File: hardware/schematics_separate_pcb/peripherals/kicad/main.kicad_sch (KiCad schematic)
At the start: 41 parts, among them IC110 74245N, IC113 7404N, IC116 74138N, IC122 7420N, IC162 7430N, IC165 7427N, IC172 74244N, IC173 74244N, IC174 74244N, IC176 74138N, IC188 7432N, IC197 74244N, IC199 74138N, IC35 7408N, IC43 7404N, IC86 74138N, J1 Conn_02x17_Odd_Even, J2 DIN41612_03x32_C_Split, J3 Conn_02x25_Odd_Even_MountingP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, U1 AS6C4008-55PCN, U10 8253, U12 74LS377, U13 16550, U14 16550, U15 AS6C4008-55PCN, U16 27C512, U17 M48Tx2, U2 AS6C4008-55PCN, U20 74LS244, U22 74HCT244, U3 AS6C4008-55PCN, U4 AS6C4008-55PCN, U5 AS6C4008-55PCN, U6 AS6C4008-55PCN, U7 AS6C4008-55PCN, U8 CY62256-70PC, X2 8mhz_osc

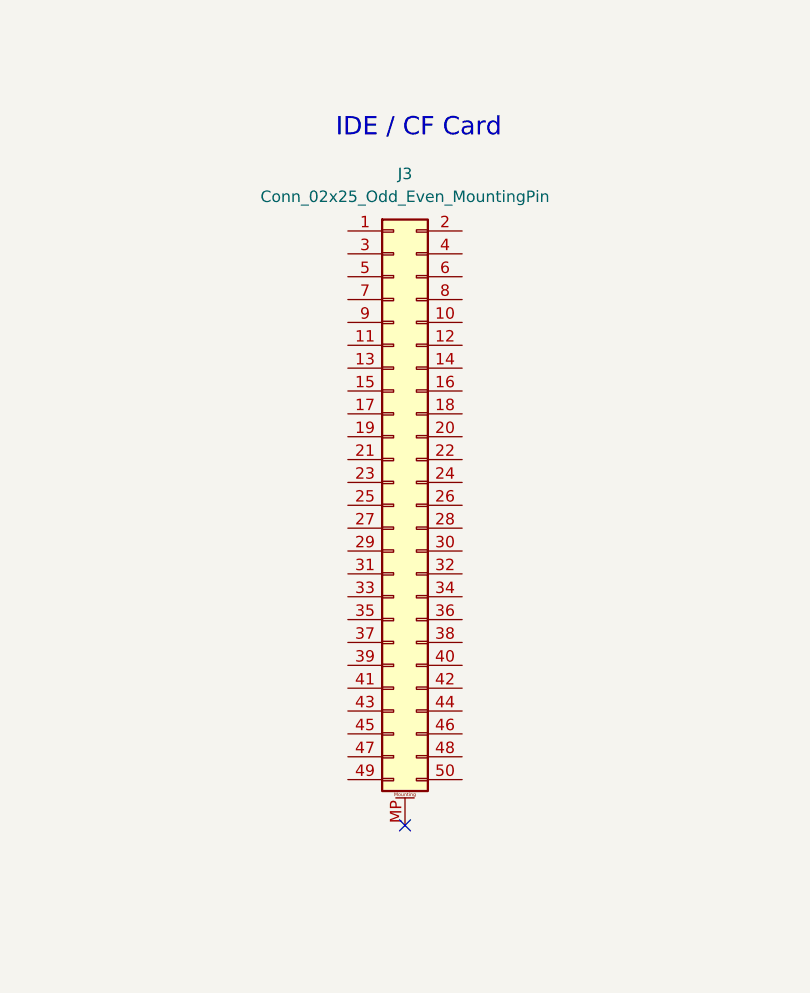
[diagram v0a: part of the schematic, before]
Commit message: improve emulator with -O3 flag
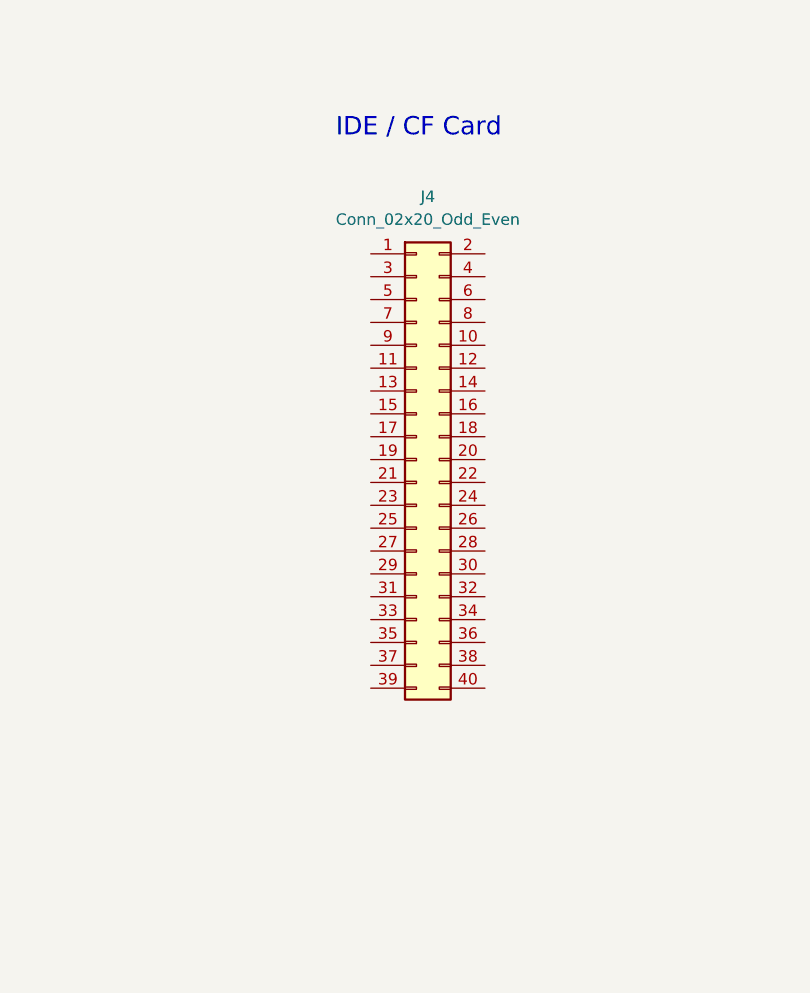
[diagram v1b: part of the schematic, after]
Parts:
- removed J3: Conn_02x25_Odd_Even_MountingPin, symbol Connector_Generic_MountingPin:Conn_02x25_Odd_Even_MountingPin
- added unit 2 of IC110
- added unit 3 of IC113
- added unit 2 of IC113
- added unit 5 of IC113
- added unit 6 of IC113
- added unit 7 of IC113
- added unit 2 of IC116
- added unit 2 of IC122
- added unit 3 of IC122
- added unit 2 of IC162
- added unit 4 of IC165
- added unit 3 of IC165
- added unit 3 of IC172
- added unit 3 of IC173
- added unit 3 of IC174
- added unit 2 of IC176
- added unit 5 of IC188
- added unit 4 of IC188
- added unit 3 of IC197
- added unit 2 of IC199
- added unit 1 of IC35
- added unit 2 of IC35
- added unit 4 of IC35
- added unit 5 of IC35
- added unit 7 of IC43
- added unit 6 of IC43
- added unit 1 of IC43
- added unit 3 of IC43
- added unit 5 of IC43
- added unit 4 of IC43
- added unit 1 of IC86
- added J4: Conn_02x20_Odd_Even, symbol Connector_Generic:Conn_02x20_Odd_Even
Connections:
- net GND: now also IC110.10 (GND), IC113.7 (GND), IC116.8 (GND), IC122.7 (GND), IC162.14 (VCC), IC165.10 (I1), IC165.14 (VCC), IC172.10 (GND), IC173.10 (GND), IC174.10 (GND), IC176.8 (GND), IC188.7 (GND), IC197.10 (GND), IC199.8 (GND), IC35.7 (GND), IC43.7 (GND); no longer IC110.10 (GND), IC113.7 (GND), IC116.8 (GND), IC122.7 (GND), IC162.14 (VCC), IC165.10 (I1), IC165.14 (VCC), IC172.10 (GND), IC173.10 (GND), IC174.10 (GND), IC176.8 (GND), IC188.7 (GND), IC197.10 (GND), IC199.8 (GND), IC35.7 (GND), IC43.7 (GND)
- net VCC: now also IC110.20 (VCC), IC113.14 (VCC), IC116.16 (VCC), IC122.12 (I2), IC122.14 (VCC), IC162.7 (GND), IC165.7 (GND), IC172.20 (VCC), IC173.20 (VCC), IC174.20 (VCC), IC176.16 (VCC), IC188.14 (VCC), IC197.20 (VCC), IC199.16 (VCC), IC35.14 (VCC), IC43.14 (VCC), IC86.6 (G1); no longer IC110.20 (VCC), IC113.14 (VCC), IC116.16 (VCC), IC122.12 (I2), IC122.14 (VCC), IC162.7 (GND), IC165.7 (GND), IC172.20 (VCC), IC173.20 (VCC), IC174.20 (VCC), IC176.16 (VCC), IC188.14 (VCC), IC197.20 (VCC), IC199.16 (VCC), IC35.14 (VCC), IC43.14 (VCC), IC86.6 (G1)
- net address_bus0: now also IC86.1 (A); no longer IC86.1 (A)
- net address_bus1: now also IC86.2 (B); no longer IC86.2 (B)
- net address_bus2: now also IC86.3 (C); no longer IC86.3 (C)
- net address_bus3: now also IC86.4 (G2A); no longer IC86.4 (G2A)
- net buffered_mem_io: now also IC113.5 (I), IC122.9 (I0); no longer IC113.5 (I), IC122.9 (I0)
- net dir: now also IC43.12 (O); no longer IC43.12 (O)
- net fdc: now also IC86.5 (G2B); no longer IC86.5 (G2B)
- net fdc_input_port_re: now also IC86.14 (Y1); no longer IC86.14 (Y1)
- net fdc_output_port_we: now also IC86.15 (Y0); no longer IC86.15 (Y0)
- net motor_en: now also IC43.10 (O); no longer IC43.10 (O)
- net rst: now also IC113.13 (I), IC165.11 (I2); no longer IC113.13 (I), IC165.11 (I2)
- net step: now also IC43.2 (O); no longer IC43.2 (O)
- net wd1770_rst: now also IC165.9 (I0); no longer IC165.9 (I0)
- net write_data: now also IC43.8 (O); no longer IC43.8 (O)
- net write_gate: now also IC43.6 (O); no longer IC43.6 (O)
- net ~{rst}: now also IC113.12 (O); no longer IC113.12 (O)
- net at IC165.6 (O): now also IC35.2 (I1); no longer IC35.2 (I1)
- net at WD1.13 (~{MR}): now also IC165.8 (O); no longer IC165.8 (O)
- net at WD1.16 (STEP): now also IC43.1 (I); no longer IC43.1 (I)
- net at WD1.20 (MO): now also IC43.11 (I); no longer IC43.11 (I)
- net at WD1.17 (DIRC): now also IC43.13 (I); no longer IC43.13 (I)
- net at WD1.21 (WG): now also IC43.5 (I); no longer IC43.5 (I)
- net at WD1.22 (WD): now also IC43.9 (I); no longer IC43.9 (I)
- net at IC113.1 (I), IC122.5 (I3), IC173.3 (Y4): now also IC35.4 (I0); no longer IC35.4 (I0)
- net at IC113.2 (O): now also IC122.13 (I3); no longer IC122.13 (I3)
- net at U16.20 (~{CE}): now also IC122.8 (O); no longer IC122.8 (O)
- net at WD1.1 (~{CS}): now also IC188.11 (O); no longer IC188.11 (O)
- net at IC188.3 (O): now also IC188.12 (I0); no longer IC188.12 (I0)
- net at IC35.8 (O): now also IC188.13 (I1); no longer IC188.13 (I1)
- net at IC165.12 (O): now also IC35.1 (I0); no longer IC35.1 (I0)
- net at IC113.8 (O): now also IC35.5 (I1); no longer IC35.5 (I1)
- net at IC116.6 (G1): now also IC35.6 (O); no longer IC35.6 (O)
- net at IC116.15 (Y0): now also IC113.3 (I); no longer IC113.3 (I)
- net at IC116.4 (G2A), IC116.5 (G2B): now also IC113.6 (O); no longer IC113.6 (O)
- net at IC199.6 (G1): now also IC113.4 (O); no longer IC113.4 (O)
- new net: IC122.10 (I1), IC122.2 (I1), IC35.3 (O)
- no-connect marks 70 -> 69
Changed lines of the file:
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@@
 	)
 	(no_connect
-		(at 683.26 1305.56)
-	)
-	(no_connect
 		(at 1285.24 1098.55)
 	)
@@
 	)
 	(symbol
-		(lib_id "Connector_Generic_MountingPin:Conn_02x25_Odd_Even_MountingPin")
-		(at 681.99 1270 0)
-		(unit 1)
-		(exclude_from_sim no)
-		(in_bom yes)
-		(on_board yes)
-		(dnp no)
-		(fields_autoplaced yes)
-		(property "Reference" "J3"
-			(at 683.26 1233.17 0)
-			(effects
-				(font
-					(size 1.27 1.27)
-				)
-			)
-		)
-		(property "Value" "Conn_02x25_Odd_Even_MountingPin"
-			(at 683.26 1235.71 0)
-			(effects
-				(font
-					(size 1.27 1.27)
-				)
-			)
-		)
-		(property "Footprint" ""
-			(at 681.99 1270 0)
-			(effects
-				(font
-					(size 1.27 1.27)
-				)
-				(hide yes)
-			)
-		)
-		(property "Datasheet" "~"
-			(at 681.99 1270 0)
-			(effects
-				(font
-					(size 1.27 1.27)
-				)
-				(hide yes)
-			)
-		)
-		(property "Description" "Generic connectable mounting pin connector, double row, 02x25, odd/even pin numbering scheme (row 1 odd numbers, row 2 even numbers), script generated (kicad-library-utils/schlib/autogen/connector/)"
-			(at 681.99 1270 0)
-			(effects
-				(font
-					(size 1.27 1.27)
-				)
-				(hide yes)
-			)
-		)
-		(pin "28"
-		)
-		(pin "24"
-		)
-		(pin "16"
-		)
-		(pin "40"
-		)
-		(pin "8"
-		)
-		(pin "2"
-		)
-		(pin "6"
-		)
-		(pin "36"
-		)
-		(pin "46"
-		)
-		(pin "39"
-		)
-		(pin "48"
-		)
-		(pin "38"
-		)
-		(pin "32"
-		)
-		(pin "1"
-		)
-		(pin "9"
-		)
-		(pin "33"
-		)
-		(pin "10"
-		)
-		(pin "44"
-		)
-		(pin "14"
-		)
-		(pin "42"
-		)
-		(pin "49"
-		)
-		(pin "41"
-		)
-		(pin "17"
-		)
-		(pin "25"
-		)
-		(pin "18"
-		)
-		(pin "43"
-		)
-		(pin "26"
-		)
-		(pin "22"
-		)
-		(pin "23"
-		)
-		(pin "37"
-		)
-		(pin "27"
-		)
-		(pin "35"
-		)
-		(pin "15"
-		)
-		(pin "29"
-		)
-		(pin "47"
-		)
-		(pin "4"
-		)
-		(pin "34"
-		)
-		(pin "12"
-		)
-		(pin "50"
-		)
-		(pin "MP"
-		)
-		(pin "19"
-		)
-		(pin "21"
-		)
-		(pin "30"
-		)
-		(pin "20"
-		)
-		(pin "5"
-		)
-		(pin "7"
-		)
-		(pin "3"
-		)
-		(pin "31"
-		)
-		(pin "13"
-		)
-		(pin "11"
-		)
-		(pin "45"
-		)
-		(instances
-			(project ""
-				(path "/8dc530de-176d-4542-9ed1-97157904b8fd"
-					(reference "J3")
-					(unit 1)
-				)
-			)
-		)
-	)
-	(symbol
 		(lib_id "power:GND")
 		(at 430.53 1203.96 0)
@@
 					(unit 1)
 				)
+			)
+		)
+	)
+	(symbol
+		(lib_id "Connector_Generic:Conn_02x20_Odd_Even")
+		(at 684.53 1264.92 0)
+		(unit 1)
+		(exclude_from_sim no)
+		(in_bom yes)
+		(on_board yes)
+		(dnp no)
+		(fields_autoplaced yes)
+		(property "Reference" "J4"
+			(at 685.8 1235.71 0)
+			(effects
+				(font
+					(size 1.27 1.27)
+				)
+			)
+		)
+		(property "Value" "Conn_02x20_Odd_Even"
+			(at 685.8 1238.25 0)
+			(effects
+				(font
+					(size 1.27 1.27)
+				)
+			)
+		)
+		(property "Footprint" ""
+			(at 684.53 1264.92 0)
+			(effects
+				(font
+					(size 1.27 1.27)
+				)
+				(hide yes)
+			)
+		)
+		(property "Datasheet" "~"
+			(at 684.53 1264.92 0)
+			(effects
+				(font
+					(size 1.27 1.27)
+				)
+				(hide yes)
+			)
+		)
+		(property "Description" "Generic connector, double row, 02x20, odd/even pin numbering scheme (row 1 odd numbers, row 2 even numbers), script generated (kicad-library-utils/schlib/autogen/connector/)"
+			(at 684.53 1264.92 0)
+			(effects
+				(font
+					(size 1.27 1.27)
+				)
+				(hide yes)
+			)
+		)
+		(pin "26"
+		)
+		(pin "28"
+		)
+		(pin "40"
+		)
+		(pin "1"
+		)
+		(pin "25"
+		)
+		(pin "30"
+		)
+		(pin "3"
+		)
+		(pin "5"
+		)
+		(pin "16"
+		)
+		(pin "32"
+		)
+		(pin "10"
+		)
+		(pin "8"
+		)
+		(pin "21"
+		)
+		(pin "39"
+		)
+		(pin "4"
+		)
+		(pin "2"
+		)
+		(pin "37"
+		)
+		(pin "34"
+		)
+		(pin "31"
+		)
+		(pin "35"
+		)
+		(pin "22"
+		)
+		(pin "29"
+		)
+		(pin "12"
+		)
+		(pin "6"
+		)
+		(pin "18"
+		)
+		(pin "27"
+		)
+		(pin "11"
+		)
+		(pin "13"
+		)
+		(pin "7"
+		)
+		(pin "24"
+		)
+		(pin "14"
+		)
+		(pin "33"
+		)
+		(pin "23"
+		)
+		(pin "20"
+		)
+		(pin "36"
+		)
+		(pin "17"
+		)
+		(pin "19"
+		)
+		(pin "15"
+		)
+		(pin "38"
+		)
+		(pin "9"
+		)
+		(instances
+			(project ""
+				(path "/8dc530de-176d-4542-9ed1-97157904b8fd"
+					(reference "J4")
+					(unit 1)
+				)
